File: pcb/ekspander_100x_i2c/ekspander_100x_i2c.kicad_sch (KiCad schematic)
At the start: 11 parts, among them J1 DG127A-5.08-06P-14-00AH, J2 DG127A-5.08-06P-14-00AH, J3 DG127A-5.08-06P-14-00AH, J4 DG127A-5.08-06P-14-00AH, U1 MCP23017_SP, U10 ITS716G, U11 LTV-847, U12 ITS716G, U9 LTV-847

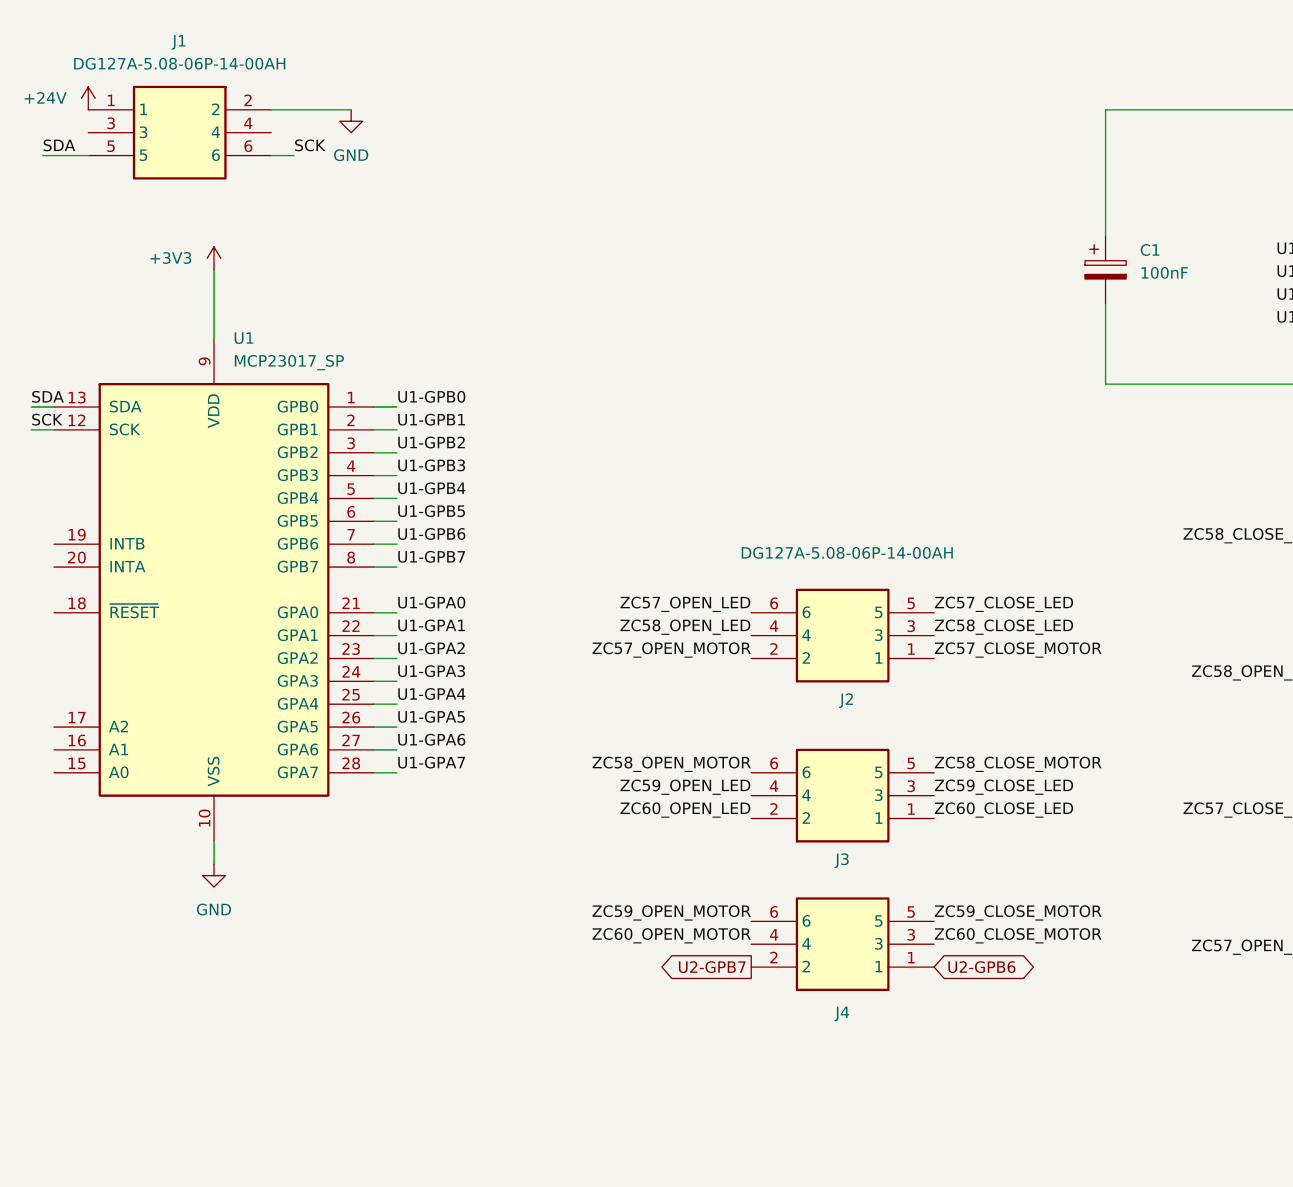
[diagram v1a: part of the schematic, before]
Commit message: Ekspander U2 - U3 - U4 update
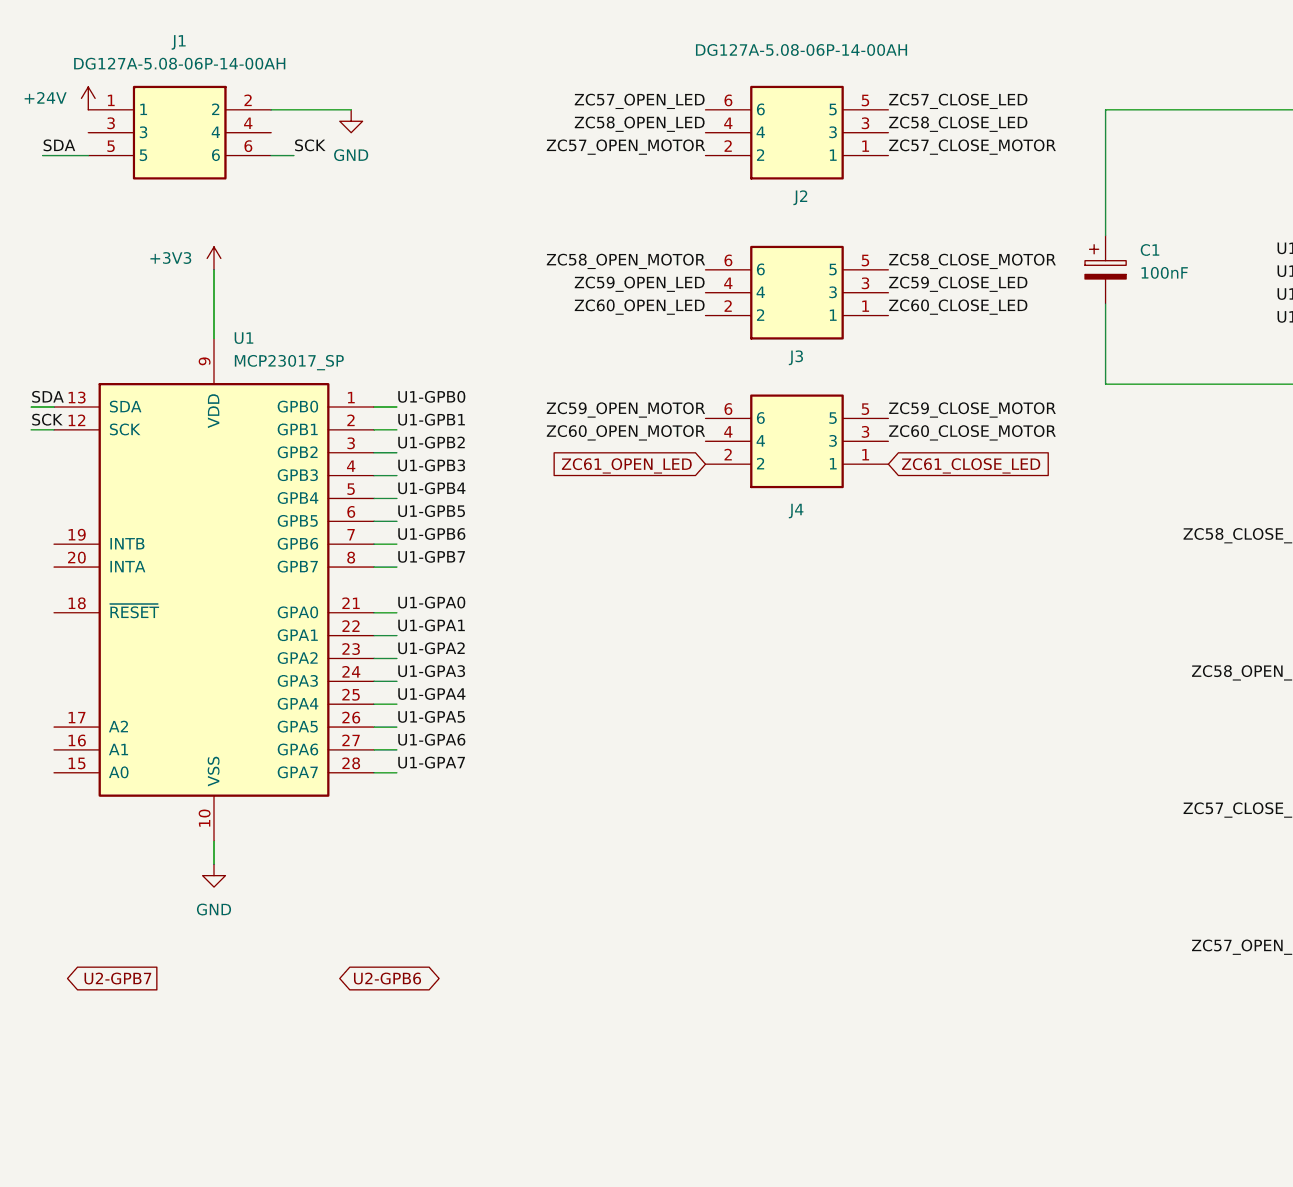
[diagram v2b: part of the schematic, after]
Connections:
- net U2-GPB6: no longer J4.1
- net U2-GPB7: no longer J4.2
- new net ZC61_CLOSE_LED: J4.1
- new net ZC61_OPEN_LED: J4.2
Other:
- moved on the sheet: J2, J3, J4
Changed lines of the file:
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@@
 	)
 	(label "ZC57_OPEN_LED"
-		(at 96.52 80.01 180)
+		(at 91.44 24.13 180)
 		(effects
 			(font
@@
 	)
 	(label "ZC60_OPEN_MOTOR"
-		(at 96.52 116.84 180)
+		(at 91.44 60.96 180)
 		(effects
 			(font
@@
 	)
 	(label "ZC60_OPEN_LED"
-		(at 96.52 102.87 180)
+		(at 91.44 46.99 180)
 		(effects
 			(font
@@
 	)
 	(label "ZC58_OPEN_MOTOR"
-		(at 96.52 97.79 180)
+		(at 91.44 41.91 180)
 		(effects
 			(font
@@
 	)
 	(label "ZC59_OPEN_MOTOR"
-		(at 96.52 114.3 180)
+		(at 91.44 58.42 180)
 		(effects
 			(font
@@
 	)
 	(label "ZC57_CLOSE_LED"
-		(at 116.84 80.01 0)
+		(at 111.76 24.13 0)
 		(effects
 			(font
@@
 	)
 	(label "ZC58_CLOSE_LED"
-		(at 116.84 82.55 0)
+		(at 111.76 26.67 0)
 		(effects
 			(font
@@
 	)
 	(label "ZC57_CLOSE_MOTOR"
-		(at 116.84 85.09 0)
+		(at 111.76 29.21 0)
 		(effects
 			(font
@@
 	)
 	(label "ZC59_OPEN_LED"
-		(at 96.52 100.33 180)
+		(at 91.44 44.45 180)
 		(effects
 			(font
@@
 	)
 	(label "ZC59_CLOSE_LED"
-		(at 116.84 100.33 0)
+		(at 111.76 44.45 0)
 		(effects
 			(font
@@
 	)
 	(label "ZC60_CLOSE_MOTOR"
-		(at 116.84 116.84 0)
+		(at 111.76 60.96 0)
 		(effects
 			(font
@@
 	)
 	(label "ZC60_CLOSE_LED"
-		(at 116.84 102.87 0)
+		(at 111.76 46.99 0)
 		(effects
 			(font
@@
 	)
 	(label "ZC59_CLOSE_MOTOR"
-		(at 116.84 114.3 0)
+		(at 111.76 58.42 0)
 		(effects
 			(font
@@
 	)
 	(label "ZC58_CLOSE_MOTOR"
-		(at 116.84 97.79 0)
+		(at 111.76 41.91 0)
 		(effects
 			(font
@@
 	)
 	(label "ZC57_OPEN_MOTOR"
-		(at 96.52 85.09 180)
+		(at 91.44 29.21 180)
 		(effects
 			(font
@@
 	)
 	(label "ZC58_OPEN_LED"
-		(at 96.52 82.55 180)
+		(at 91.44 26.67 180)
 		(effects
 			(font
@@
 		)
 	)
+	(global_label "U2-GPB6"
+		(shape bidirectional)
+		(at 50.8 120.65 0)
+		(fields_autoplaced yes)
+		(effects
+			(font
+				(size 1.27 1.27)
+			)
+			(justify left)
+		)
+		(property "Intersheetrefs" "${INTERSHEET_REFS}"
+			(at 64.0284 120.65 0)
+			(effects
+				(font
+					(size 1.27 1.27)
+				)
+				(justify left)
+				(hide yes)
+			)
+		)
+	)
 	(global_label "U3-GPB6"
 		(shape bidirectional)
@@
 		)
 	)
-	(global_label "SCK"
-		(shape bidirectional)
-		(at 35.56 158.75 180)
+	(global_label "ZC61_OPEN_LED"
+		(shape input)
+		(at 91.44 63.5 180)
 		(fields_autoplaced yes)
 		(effects
@@
 		)
 		(property "Intersheetrefs" "${INTERSHEET_REFS}"
-			(at 27.714 158.75 0)
+			(at 73.094 63.5 0)
 			(effects
 				(font
@@
 	(global_label "U2-GPB7"
 		(shape output)
-		(at 96.52 119.38 180)
+		(at 30.48 120.65 180)
 		(fields_autoplaced yes)
 		(effects
@@
 		)
 		(property "Intersheetrefs" "${INTERSHEET_REFS}"
-			(at 84.4029 119.38 0)
+			(at 18.3629 120.65 0)
 			(effects
 				(font
@@
 		)
 	)
-	(global_label "U3-GPB4"
+	(global_label "SCK"
 		(shape bidirectional)
-		(at 55.88 158.75 180)
+		(at 35.56 158.75 180)
 		(fields_autoplaced yes)
 		(effects
@@
 		)
 		(property "Intersheetrefs" "${INTERSHEET_REFS}"
-			(at 42.6516 158.75 0)
+			(at 27.714 158.75 0)
 			(effects
 				(font
@@
 		)
 	)
-	(global_label "U2-GPB6"
-		(shape bidirectional)
-		(at 22.86 166.37 0)
+	(global_label "ZC61_CLOSE_LED"
+		(shape input)
+		(at 111.76 63.5 0)
 		(fields_autoplaced yes)
 		(effects
@@
 		)
 		(property "Intersheetrefs" "${INTERSHEET_REFS}"
-			(at 36.0884 166.37 0)
+			(at 131.0131 63.5 0)
 			(effects
 				(font
@@
 		)
 	)
+	(global_label "U3-GPB4"
+		(shape bidirectional)
+		(at 55.88 158.75 180)
+		(fields_autoplaced yes)
+		(effects
+			(font
+				(size 1.27 1.27)
+			)
+			(justify right)
+		)
+		(property "Intersheetrefs" "${INTERSHEET_REFS}"
+			(at 42.6516 158.75 0)
+			(effects
+				(font
+					(size 1.27 1.27)
+				)
+				(justify right)
+				(hide yes)
+			)
+		)
+	)
 	(global_label "U2-GPB6"
 		(shape bidirectional)
-		(at 116.84 119.38 0)
+		(at 22.86 166.37 0)
 		(fields_autoplaced yes)
 		(effects
@@
 		)
 		(property "Intersheetrefs" "${INTERSHEET_REFS}"
-			(at 130.0684 119.38 0)
+			(at 36.0884 166.37 0)
 			(effects
 				(font
@@
 	(symbol
 		(lib_id "1_tme:DG127A-5.08-06P-14-00AH")
-		(at 96.52 85.09 0)
+		(at 91.44 29.21 0)
 		(mirror x)
 		(unit 1)
@@
 		(dnp no)
 		(property "Reference" "J2"
-			(at 107.188 89.662 0)
+			(at 102.108 33.782 0)
 			(effects
 				(font
@@
 		)
 		(property "Value" "DG127A-5.08-06P-14-00AH"
-			(at 107.188 73.406 0)
+			(at 102.108 17.526 0)
 			(effects
 				(font
@@
 		)
 		(property "Footprint" "DG127A50806P1400AH"
-			(at 113.03 -9.83 0)
+			(at 107.95 -65.71 0)
 			(effects
 				(font
@@
 		)
 		(property "Datasheet" "https://www.degson.com/index.php?a=downloadFile&id=1094971&name=%27ZmlsZTQ=%27&lang=en"
-			(at 113.03 -109.83 0)
+			(at 107.95 -165.71 0)
 			(effects
 				(font
@@
 		)
 		(property "Description" "PCB terminal block; angled 90; 5.08mm; ways: 6; on PCBs; terminal"
-			(at 96.52 85.09 0)
+			(at 91.44 29.21 0)
 			(effects
 				(font
@@
 		)
 		(property "Height" "19.41"
-			(at 113.03 -309.83 0)
+			(at 107.95 -365.71 0)
 			(effects
 				(font
@@
 		)
 		(property "TME Electronic Components Part Number" ""
-			(at 113.03 -409.83 0)
+			(at 107.95 -465.71 0)
 			(effects
 				(font
@@
 		)
 		(property "TME Electronic Components Price/Stock" ""
-			(at 113.03 -509.83 0)
+			(at 107.95 -565.71 0)
 			(effects
 				(font
@@
 		)
 		(property "Manufacturer_Name" "Degson"
-			(at 113.03 -609.83 0)
+			(at 107.95 -665.71 0)
 			(effects
 				(font
@@
 		)
 		(property "Manufacturer_Part_Number" "DG127A-5.08-06P-14-00AH"
-			(at 113.03 -709.83 0)
+			(at 107.95 -765.71 0)
 			(effects
 				(font
@@
 	(symbol
 		(lib_id "1_tme:DG127A-5.08-06P-14-00AH")
-		(at 96.52 119.38 0)
+		(at 91.44 63.5 0)
 		(mirror x)
 		(unit 1)
@@
 		(dnp no)
 		(property "Reference" "J4"
-			(at 106.68 124.46 0)
+			(at 101.6 68.58 0)
 			(effects
 				(font
@@
 		)
 		(property "Value" "DG127A-5.08-06P-14-00AH"
-			(at 106.68 124.46 0)
+			(at 101.6 68.58 0)
 			(effects
 				(font
@@
 		)
 		(property "Footprint" "DG127A50806P1400AH"
-			(at 113.03 24.46 0)
+			(at 107.95 -31.42 0)
 			(effects
 				(font
@@
 		)
 		(property "Datasheet" "https://www.degson.com/index.php?a=downloadFile&id=1094971&name=%27ZmlsZTQ=%27&lang=en"
-			(at 113.03 -75.54 0)
+			(at 107.95 -131.42 0)
 			(effects
 				(font
@@
 		)
 		(property "Description" "PCB terminal block; angled 90; 5.08mm; ways: 6; on PCBs; terminal"
-			(at 96.52 119.38 0)
+			(at 91.44 63.5 0)
 			(effects
 				(font
@@
 		)
 		(property "Height" "19.41"
-			(at 113.03 -275.54 0)
+			(at 107.95 -331.42 0)
 			(effects
 				(font
@@
 		)
 		(property "TME Electronic Components Part Number" ""
-			(at 113.03 -375.54 0)
+			(at 107.95 -431.42 0)
 			(effects
 				(font
@@
 		)
 		(property "TME Electronic Components Price/Stock" ""
-			(at 113.03 -475.54 0)
+			(at 107.95 -531.42 0)
 			(effects
 				(font
@@
 		)
 		(property "Manufacturer_Name" "Degson"
-			(at 113.03 -575.54 0)
+			(at 107.95 -631.42 0)
 			(effects
 				(font
@@
 		)
 		(property "Manufacturer_Part_Number" "DG127A-5.08-06P-14-00AH"
-			(at 113.03 -675.54 0)
+			(at 107.95 -731.42 0)
 			(effects
 				(font
@@
 	(symbol
 		(lib_id "1_tme:DG127A-5.08-06P-14-00AH")
-		(at 96.52 102.87 0)
+		(at 91.44 46.99 0)
 		(mirror x)
 		(unit 1)
@@
 		(dnp no)
 		(property "Reference" "J3"
-			(at 106.68 107.442 0)
+			(at 101.6 51.562 0)
 			(effects
 				(font
@@
 		)
 		(property "Value" "DG127A-5.08-06P-14-00AH"
-			(at 106.68 107.95 0)
+			(at 101.6 52.07 0)
 			(effects
 				(font
@@
 		)
 		(property "Footprint" "DG127A50806P1400AH"
-			(at 113.03 7.95 0)
+			(at 107.95 -47.93 0)
 			(effects
 				(font
@@
 		)
 		(property "Datasheet" "https://www.degson.com/index.php?a=downloadFile&id=1094971&name=%27ZmlsZTQ=%27&lang=en"
-			(at 113.03 -92.05 0)
+			(at 107.95 -147.93 0)
 			(effects
 				(font
@@
 		)
 		(property "Description" "PCB terminal block; angled 90; 5.08mm; ways: 6; on PCBs; terminal"
-			(at 96.52 102.87 0)
+			(at 91.44 46.99 0)
 			(effects
 				(font
@@
 		)
 		(property "Height" "19.41"
-			(at 113.03 -292.05 0)
+			(at 107.95 -347.93 0)
 			(effects
 				(font
@@
 		)
 		(property "TME Electronic Components Part Number" ""
-			(at 113.03 -392.05 0)
+			(at 107.95 -447.93 0)
 			(effects
 				(font
@@
 		)
 		(property "TME Electronic Components Price/Stock" ""
-			(at 113.03 -492.05 0)
+			(at 107.95 -547.93 0)
 			(effects
 				(font
@@
 		)
 		(property "Manufacturer_Name" "Degson"
-			(at 113.03 -592.05 0)
+			(at 107.95 -647.93 0)
 			(effects
 				(font
@@
 		)
 		(property "Manufacturer_Part_Number" "DG127A-5.08-06P-14-00AH"
-			(at 113.03 -692.05 0)
+			(at 107.95 -747.93 0)
 			(effects
 				(font

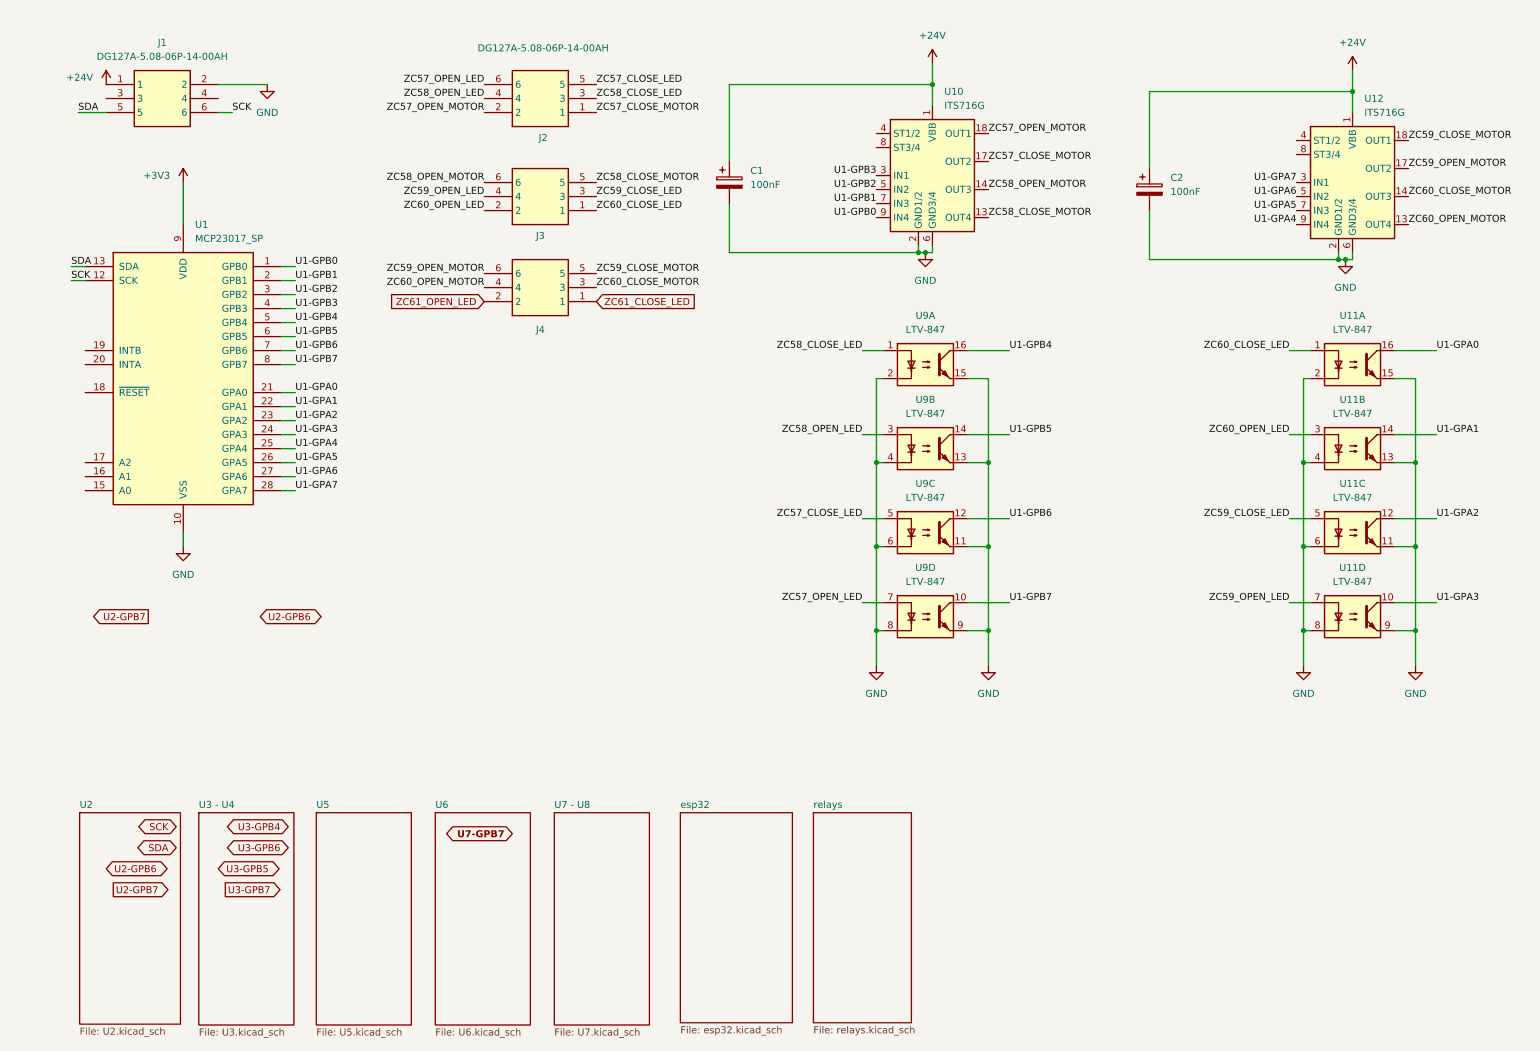
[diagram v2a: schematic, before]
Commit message: Ekspander 24V update
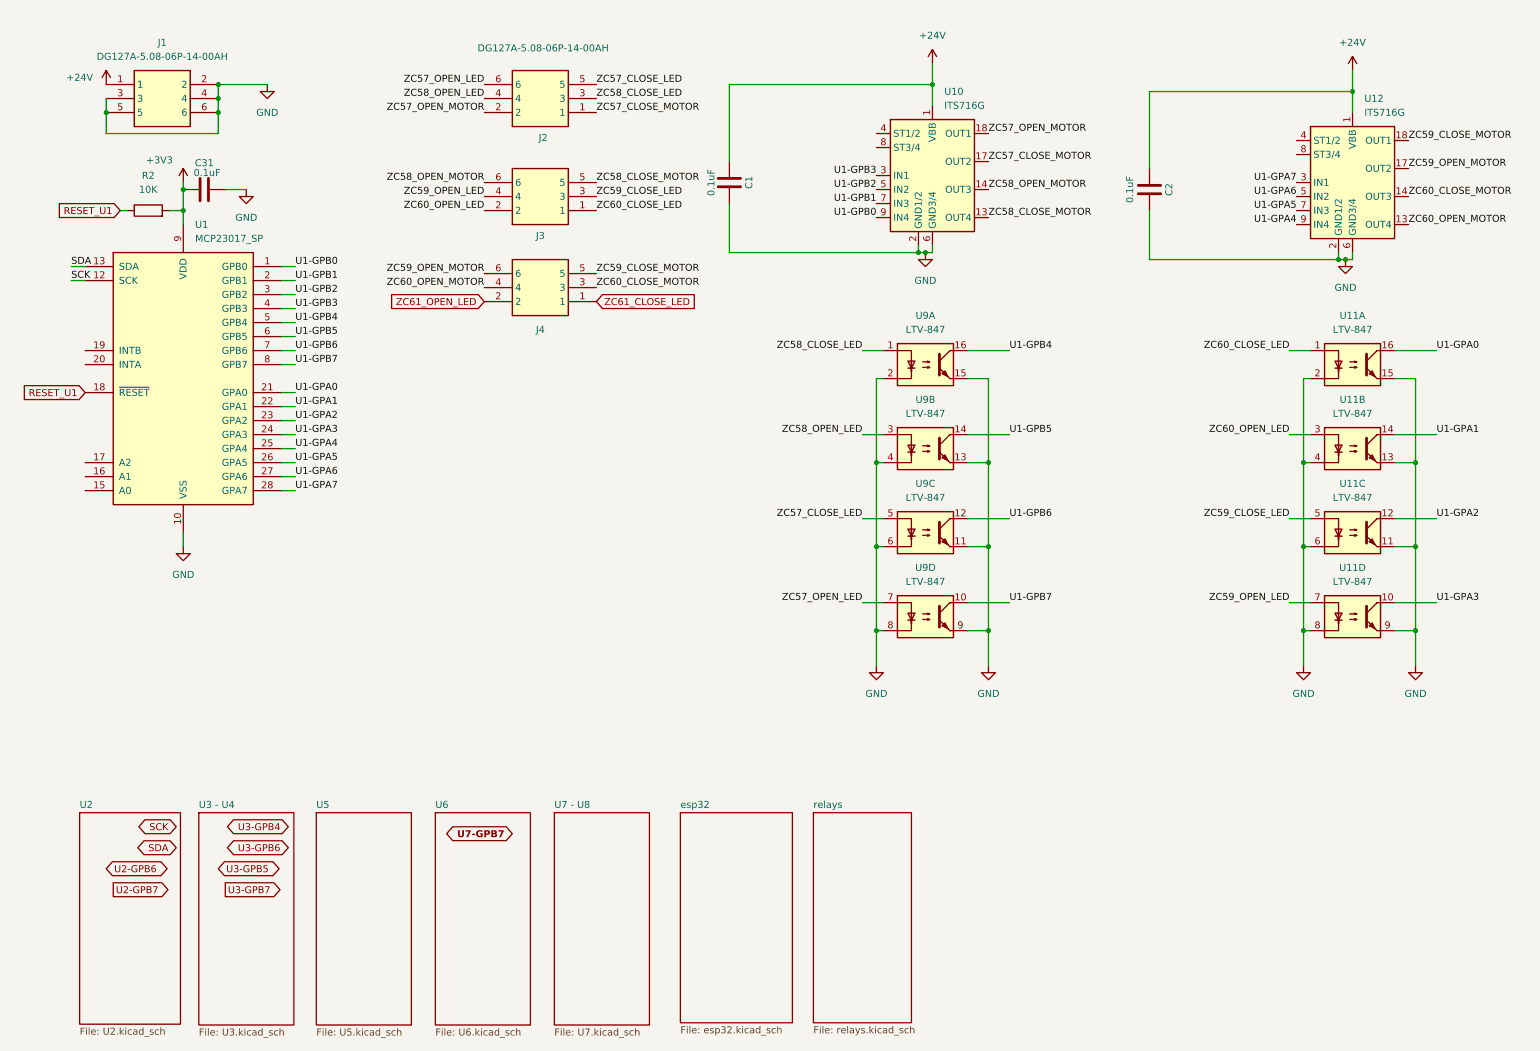
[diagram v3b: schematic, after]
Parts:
- removed C1, C2: 100nF, Capacitor_THT:C_Disc_D3.0mm_W2.0mm_P2.50mm, symbol Device:C_Polarized
- added C1, C2, C31: 0.1uF, Capacitor_SMD:C_0805_2012Metric_Pad1.18x1.45mm_HandSolder, symbol Device:C
- added R2: 10K, PCM_Resistor_SMD_AKL:R_0805_2012Metric_Pad1.20x1.40mm_HandSolder, symbol Device:R
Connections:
- net +24V: now also C1.1, C2.1
- net +3V3: now also C31.1, R2.2
- net GND: now also J1.3, J1.4, J1.5, J1.6, C1.2, C2.2, C31.2
- net SCK: no longer J1.6
- net SDA: no longer J1.5
- net RESET_U1: now reaches U1.18 (~{RESET})
- net RESET_U1: now also R2.1
